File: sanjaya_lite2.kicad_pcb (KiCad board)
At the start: 2 copper layers, 104 parts, among them J1 Conn_12V, J10 Adap_In, J11 DCDC_Bypass, J12 Conn_RS485, J13 Bat_Bypass+, J14 J_Bat, J15 Conn_420_1, J16 Conn_420_2, J17 Conn_420_3, J18 Conn_420_4, J19 Volt_check_5V, J2 J_SW_Esp, J20 Pwr_SW, J21 J_SW_Sim800, J3 Conn_5V, J4 J_LED, J5 Conn_Bat, J6 Conn_I2C, J7 Conn_SPI, J8 Conn_I2C, J9 J_UART_DBG, Q1 PMOS_SI2369DS, Q2 BSS138, Q3 BSS138, SW1 SW_Reset, SW2 SW_Boot, U1 ESP32-WROOM-32, U2 MCP1700-3302E_SOT23, U3 SN65HVD75DR, U5 MCP3428

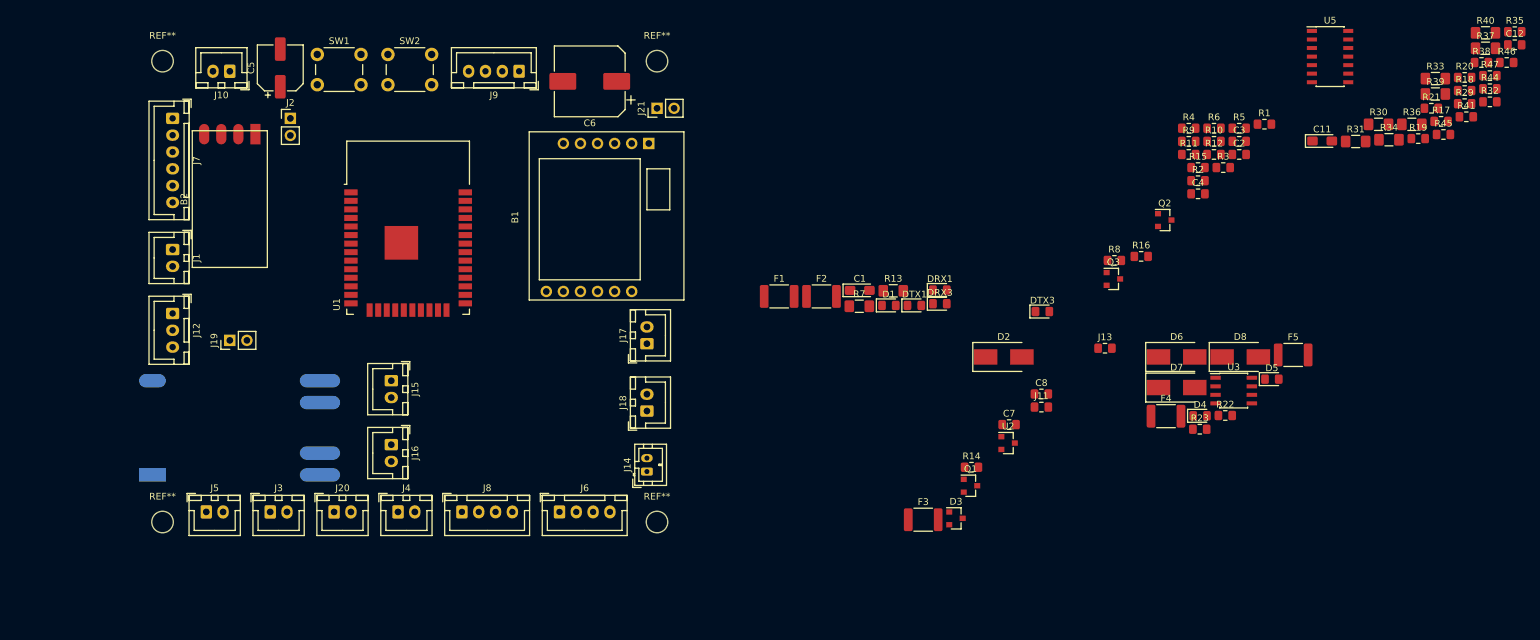
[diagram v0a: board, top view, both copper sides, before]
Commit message: Basic board layout with connectors and large components done
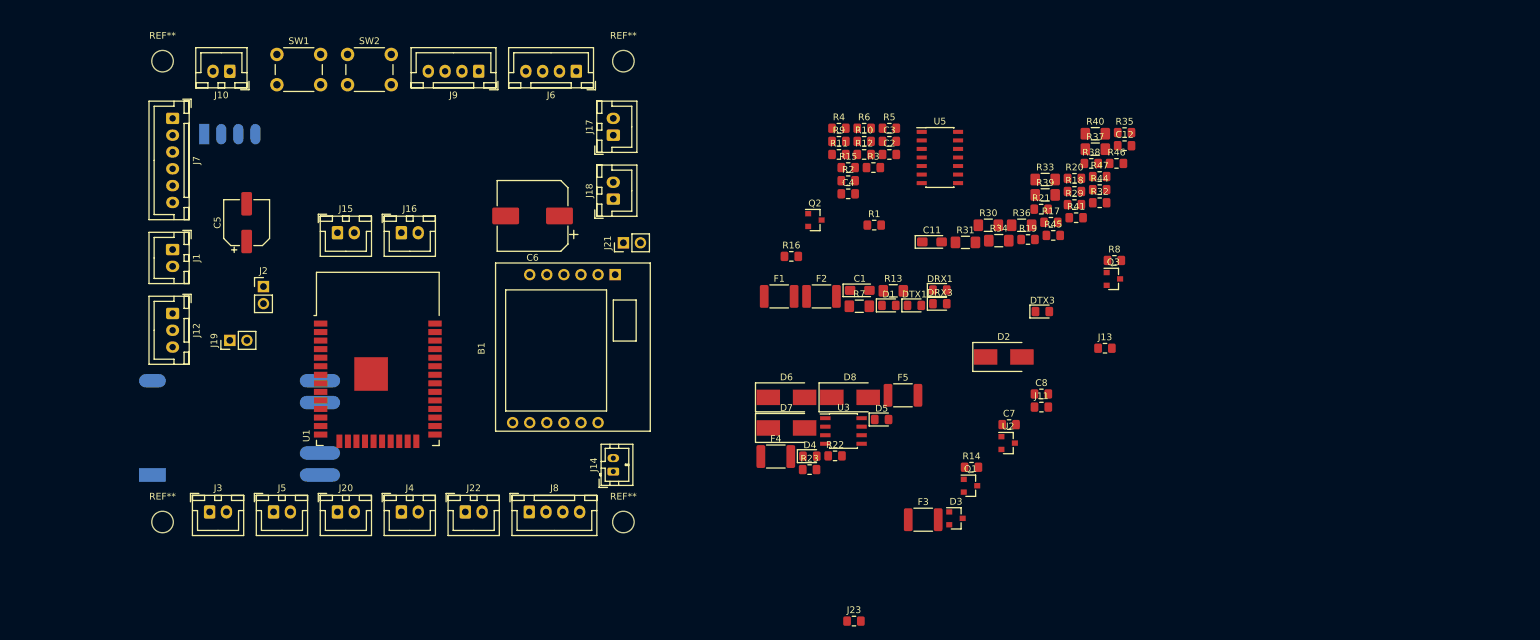
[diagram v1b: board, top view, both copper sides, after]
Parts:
- added J22: UART_Sim800, Connector_JST:JST_XH_B02B-XH-A_1x02_P2.50mm_Vertical, F.Cu at (135.0, 127.0)
- added J23: Bat_Prot_Bypass, Resistor_SMD:R_0805_2012Metric_Pad1.15x1.40mm_HandSolder, F.Cu at (192.8, 143.2)
- B2: moved to B.Cu
- J1: value Conn_12V -> 12V_Out
- J13: value Bat_Bypass+ -> Bat_Bypass
- J3: value Conn_5V -> 5V_Out
- J5: value Conn_Bat -> VBat_Out
- moved J6 65.5 mm to (151.5, 61.5), turned to 180 degrees
- moved C11 59.9 mm to (204.4, 86.9)
- moved R17 59.9 mm to (222.0, 83.9)
- moved R18 59.9 mm to (225.5, 79.4)
- moved R20 59.9 mm to (225.5, 77.4)
- moved R29 59.9 mm to (225.5, 81.3)
- moved R32 59.9 mm to (229.3, 81.0)
- moved R34 59.9 mm to (214.3, 86.7)
- moved R38 59.9 mm to (228.0, 75.2)
- moved R41 59.9 mm to (225.8, 83.3)
- moved R44 59.9 mm to (229.3, 79.1)
- moved R46 59.9 mm to (231.8, 75.2)
- moved R47 59.9 mm to (229.3, 77.1)
- moved U5 59.9 mm to (205.5, 74.3)
- moved C12 59.9 mm to (233.0, 72.6)
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
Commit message: Made some changes to the layout. It is still incomplete
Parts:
- added G***: LOGO, Custom Silkscreens:bodhileafLogoAndText, F.Cu at (121.0, 119.4)
- added R24: 120, Resistor_SMD:R_0805_2012Metric_Pad1.15x1.40mm_HandSolder, F.Cu at (74.0, 106.5)
- added REF**: TestPoint_THTPad_D2.0mm_Drill1.0mm, TestPoint:TestPoint_THTPad_D2.0mm_Drill1.0mm, F.Cu at (110.5, 106.0)
- C1, C2, C3, C4, R1, R13, R2, R3, R4, R5, R6: moved to B.Cu
- U1: footprint RF_Module:ESP32-WROOM-32 -> Custom Boards:ESP32-WROOM-32_Handsolder
- moved D6 110.6 mm to (72.5, 101.0)
- moved D1 98.5 mm to (99.5, 100.0), turned to 90 degrees
- moved C1 97.8 mm to (96.0, 100.5), turned to 270 degrees
- moved R1 94.6 mm to (102.5, 100.0), turned to 270 degrees
- moved C2 94.2 mm to (107.5, 100.0), turned to 270 degrees
- moved R3 92.9 mm to (106.0, 100.0), turned to 270 degrees
- moved R5 91.9 mm to (116.5, 112.5), turned to 270 degrees
- moved R6 91.3 mm to (113.5, 112.5), turned to 90 degrees
- moved C3 90.5 mm to (112.0, 100.0), turned to 270 degrees
- moved C4 87.8 mm to (110.5, 112.5), turned to 270 degrees
- moved R4 86.9 mm to (109.0, 100.0), turned to 90 degrees
- moved DTX3 86.9 mm to (134.0, 93.0), turned to 90 degrees
- moved Q3 86.5 mm to (145.4, 101.7)
- moved R2 75.0 mm to (129.5, 119.4), turned to 270 degrees
- moved F5 71.5 mm to (129.5, 121.0)
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
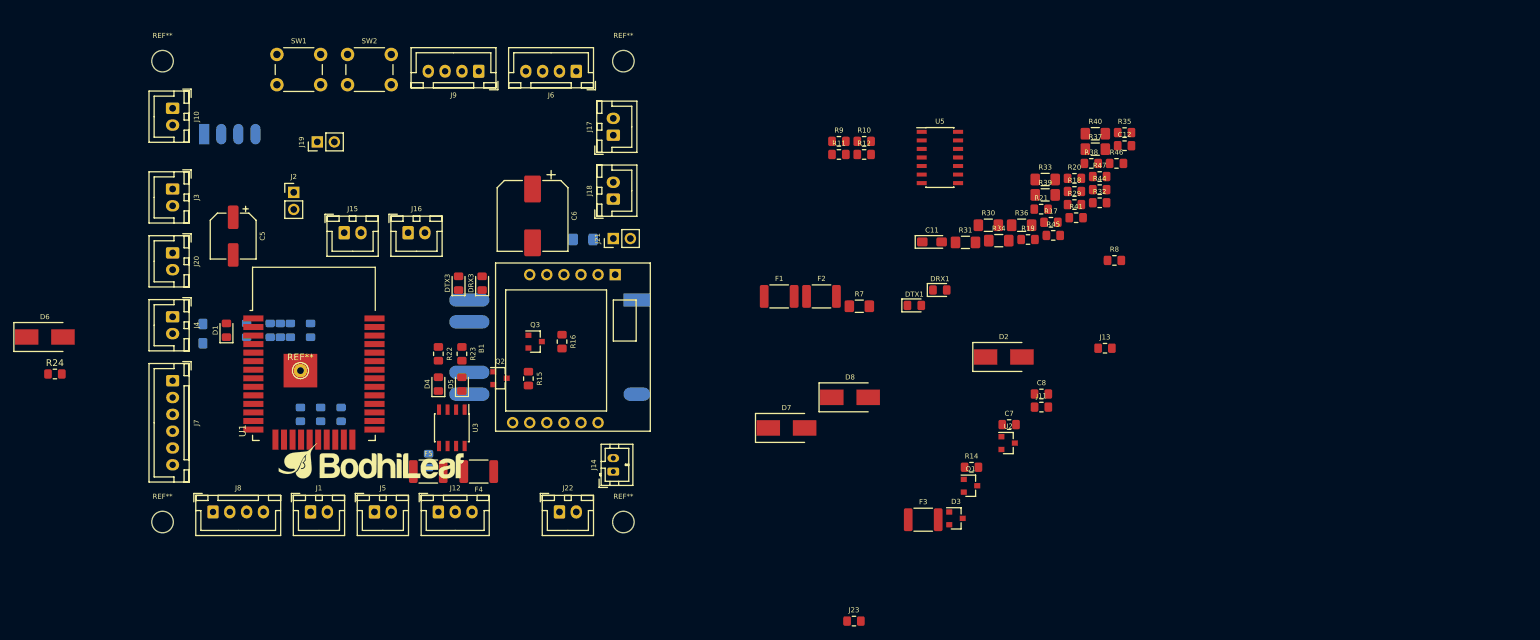
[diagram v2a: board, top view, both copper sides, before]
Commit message: Most of the layout done. Some power supply related components are the only ones remaining
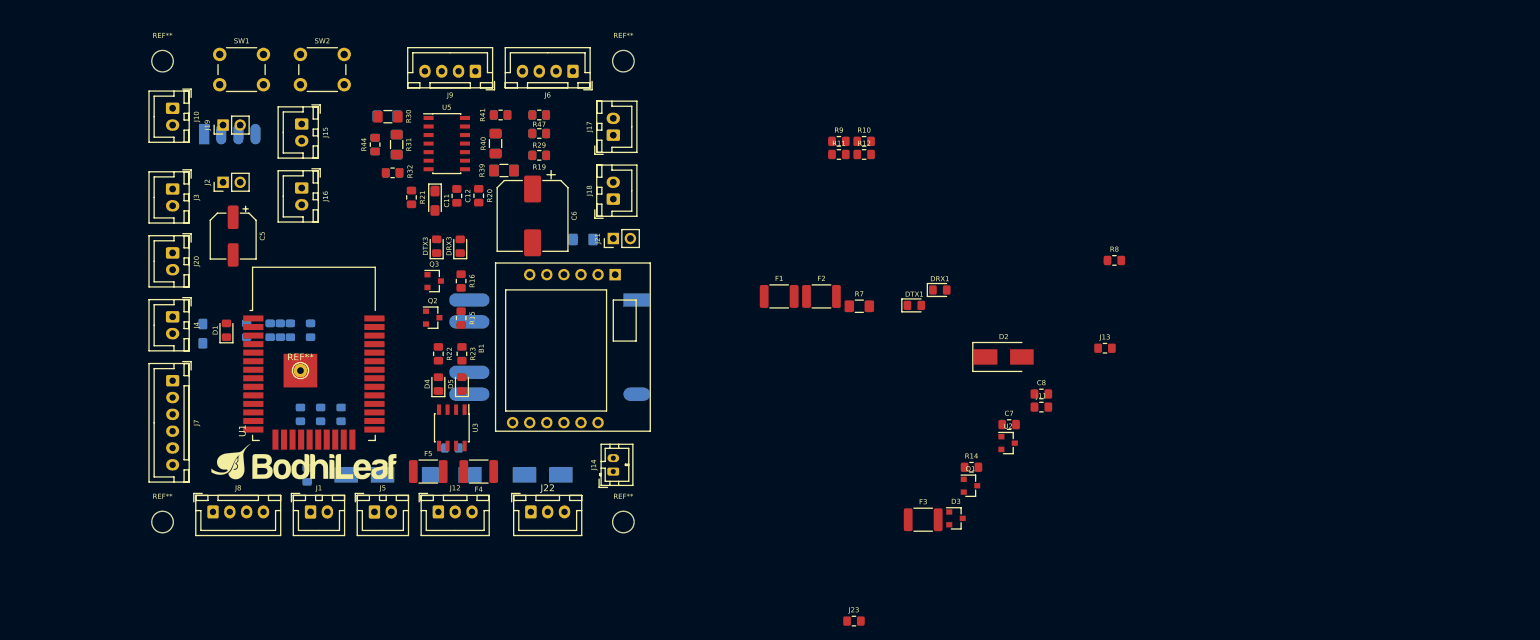
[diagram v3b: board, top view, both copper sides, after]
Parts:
- D6, D7, D8, R17, R18, R24, R33, R34, R35, R36, R37, R38, R45, R46: moved to B.Cu
- J22: footprint Connector_JST:JST_XH_B02B-XH-A_1x02_P2.50mm_Vertical -> Connector_JST:JST_XH_B03B-XH-A_1x03_P2.50mm_Vertical
- moved R35 109.0 mm to (124.2, 76.6)
- moved R44 107.9 mm to (121.6, 72.4), turned to 90 degrees
- moved R32 105.2 mm to (124.2, 76.6)
- moved R45 101.7 mm to (121.6, 72.4), turned to 270 degrees
- moved C12 99.5 mm to (133.8, 80.0), turned to 270 degrees
- moved R33 98.2 mm to (123.4, 68.2)
- moved R21 93.6 mm to (127.0, 80.2), turned to 270 degrees
- moved R30 90.7 mm to (123.5, 68.2)
- moved R34 90.6 mm to (124.8, 72.4), turned to 270 degrees
- moved R40 89.2 mm to (139.5, 72.2), turned to 90 degrees
- moved R37 89.2 mm to (139.5, 72.2), turned to 90 degrees
- moved R20 88.6 mm to (137.0, 80.0), turned to 270 degrees
- moved R38 88.1 mm to (140.2, 68.0)
- moved R41 86.9 mm to (140.2, 68.0)
- moved R46 86.1 mm to (146.0, 68.0)
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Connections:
- J22 pad 1: Net-(J22-Pad1) -> /GND_Supply
- Q3 pad 3: Net-(J22-Pad1) -> Net-(J22-Pad3)
- U1 pad 13: Net-(J22-Pad1) -> Net-(J22-Pad3)

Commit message: First layout draft
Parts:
- C7, C8, D3, F1, F2, J11, J13, J23, Q1, R10, R11, R12, R14, R7, R8, U2: moved to B.Cu
- moved R8 135.6 mm to (96.0, 95.5), turned to 270 degrees
- moved J13 135.4 mm to (96.5, 80.5), turned to 90 degrees
- moved J11 124.5 mm to (100.0, 80.5), turned to 270 degrees
- moved F3 118.8 mm to (100.0, 69.0), turned to 180 degrees
- moved D2 118.8 mm to (100.0, 74.5)
- moved Q1 115.1 mm to (108.0, 70.0), turned to 90 degrees
- moved D3 113.8 mm to (108.0, 73.5), turned to 180 degrees
- moved R14 111.3 mm to (108.0, 76.5), turned to 180 degrees
- moved R9 101.5 mm to (97.5, 112.5), turned to 180 degrees
- moved R7 96.5 mm to (98.0, 109.5)
- moved C8 95.7 mm to (125.0, 112.0), turned to 180 degrees
- moved R12 94.3 mm to (107.0, 109.5), turned to 90 degrees
- moved C7 91.3 mm to (125.0, 105.0), turned to 180 degrees
- moved U2 91.1 mm to (125.0, 108.5)
- moved DRX1 82.3 mm to (123.5, 87.5), turned to 90 degrees
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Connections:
- DRX3 pad 1: Net-(B1-Pad5) -> Net-(DRX3-Pad1)
- DRX3 pad 2: Net-(DRX3-Pad2) -> Net-(B1-Pad12)
- DTX3 pad 1: Net-(B1-Pad4) -> Net-(DTX3-Pad1)
- DTX3 pad 2: Net-(DTX3-Pad2) -> Net-(B1-Pad12)
- R15 pad 1: Net-(B1-Pad12) -> Net-(DTX3-Pad1)
- R15 pad 2: Net-(DTX3-Pad2) -> Net-(B1-Pad4)
- R16 pad 1: Net-(B1-Pad12) -> Net-(DRX3-Pad1)
- R16 pad 2: Net-(DRX3-Pad2) -> Net-(B1-Pad5)

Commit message: Created a 1A net class
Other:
- net class 1A_Carrier added: clearance 0.4, trace_width 0.5, via_dia 1, via_drill 0.5
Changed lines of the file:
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@@
     (37 F.SilkS user)
     (38 B.Mask user)
-    (39 F.Mask user)
+    (39 F.Mask user hide)
     (40 Dwgs.User user)
     (41 Cmts.User user)
@@
     (45 Margin user)
     (46 B.CrtYd user)
-    (47 F.CrtYd user)
+    (47 F.CrtYd user hide)
     (48 B.Fab user)
     (49 F.Fab user)
@@
     (solder_mask_min_width 0.25)
     (aux_axis_origin 0 0)
-    (visible_elements FFFFF77F)
+    (visible_elements FFFFFF7F)
     (pcbplotparams
       (layerselection 0x010fc_ffffffff)
@@
     (uvia_dia 0.3)
     (uvia_drill 0.1)
-    (add_net /12V_Out)
-    (add_net /5V_Out)
     (add_net /BOOT_IO0)
     (add_net /BOOT_IO2)
@@
     (add_net /SCLK)
     (add_net /SDA)
-    (add_net /Sim800_I_Sense+)
-    (add_net /Sim800_I_Sense-)
     (add_net /Sim800_RST)
     (add_net /rs485/A)
@@
     (add_net "Net-(B1-Pad5)")
     (add_net "Net-(B2-Pad3)")
-    (add_net "Net-(B2-Pad4)")
-    (add_net "Net-(B3-Pad4)")
-    (add_net "Net-(B3-Pad5)")
-    (add_net "Net-(B3-Pad6)")
     (add_net "Net-(C3-Pad1)")
     (add_net "Net-(C4-Pad1)")
     (add_net "Net-(D1-Pad2)")
-    (add_net "Net-(D2-Pad1)")
     (add_net "Net-(D3-Pad2)")
     (add_net "Net-(D4-Pad2)")
@@
     (add_net "Net-(DTX1-Pad2)")
     (add_net "Net-(DTX3-Pad1)")
-    (add_net "Net-(F1-Pad2)")
-    (add_net "Net-(F2-Pad2)")
-    (add_net "Net-(F3-Pad2)")
     (add_net "Net-(F4-Pad2)")
     (add_net "Net-(F5-Pad2)")
@@
     (add_net "Net-(R33-Pad2)")
   )
+  (net_class 1A_Carrier ""
+    (clearance 0.4)
+    (trace_width 0.5)
+    (via_dia 1)
+    (via_drill 0.5)
+    (uvia_dia 0.3)
+    (uvia_drill 0.1)
+    (add_net /12V_Out)
+    (add_net /5V_Out)
+    (add_net /Sim800_I_Sense+)
+    (add_net /Sim800_I_Sense-)
+    (add_net "Net-(B2-Pad4)")
+    (add_net "Net-(B3-Pad4)")
+    (add_net "Net-(B3-Pad5)")
+    (add_net "Net-(B3-Pad6)")
+    (add_net "Net-(D2-Pad1)")
+    (add_net "Net-(F1-Pad2)")
+    (add_net "Net-(F2-Pad2)")
+    (add_net "Net-(F3-Pad2)")
+  )
   (module "Custom Boards:TP4056_Module" (layer B.Cu)

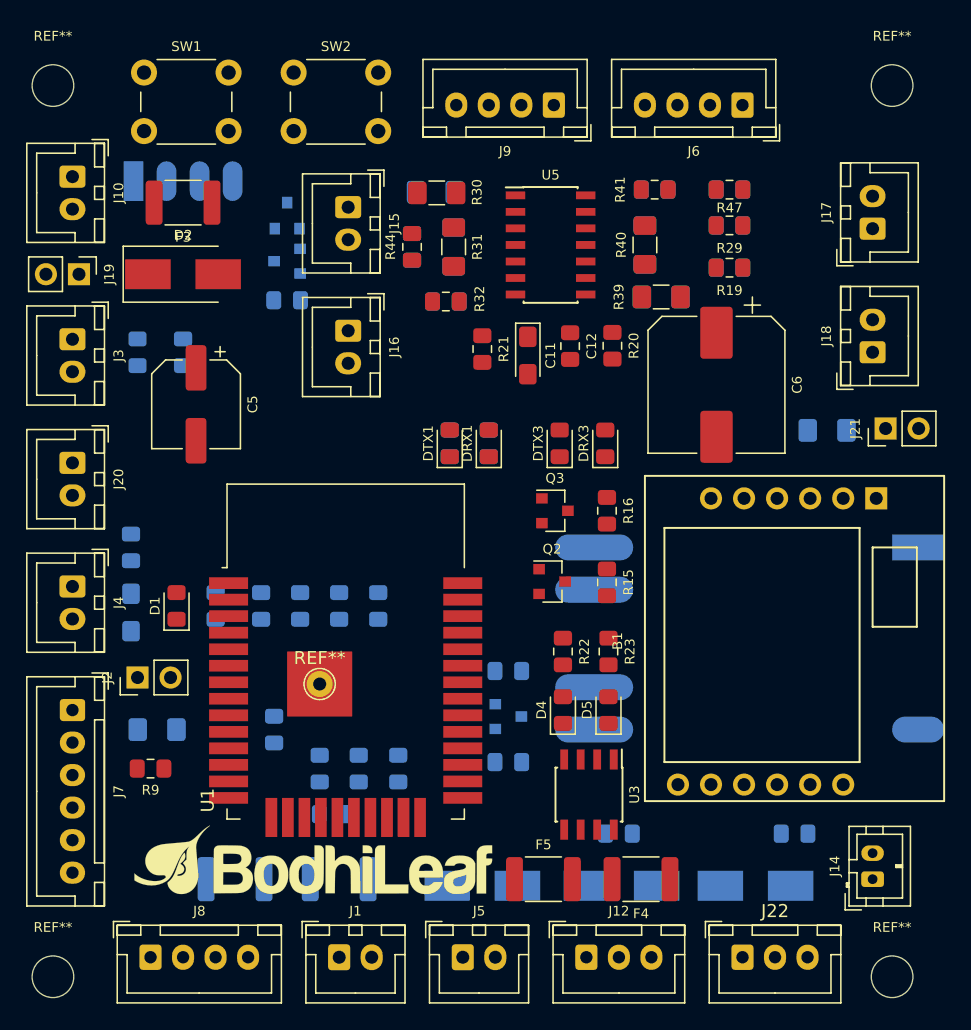
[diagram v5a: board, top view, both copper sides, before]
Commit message: Some routing done. Minor changes to schematics.
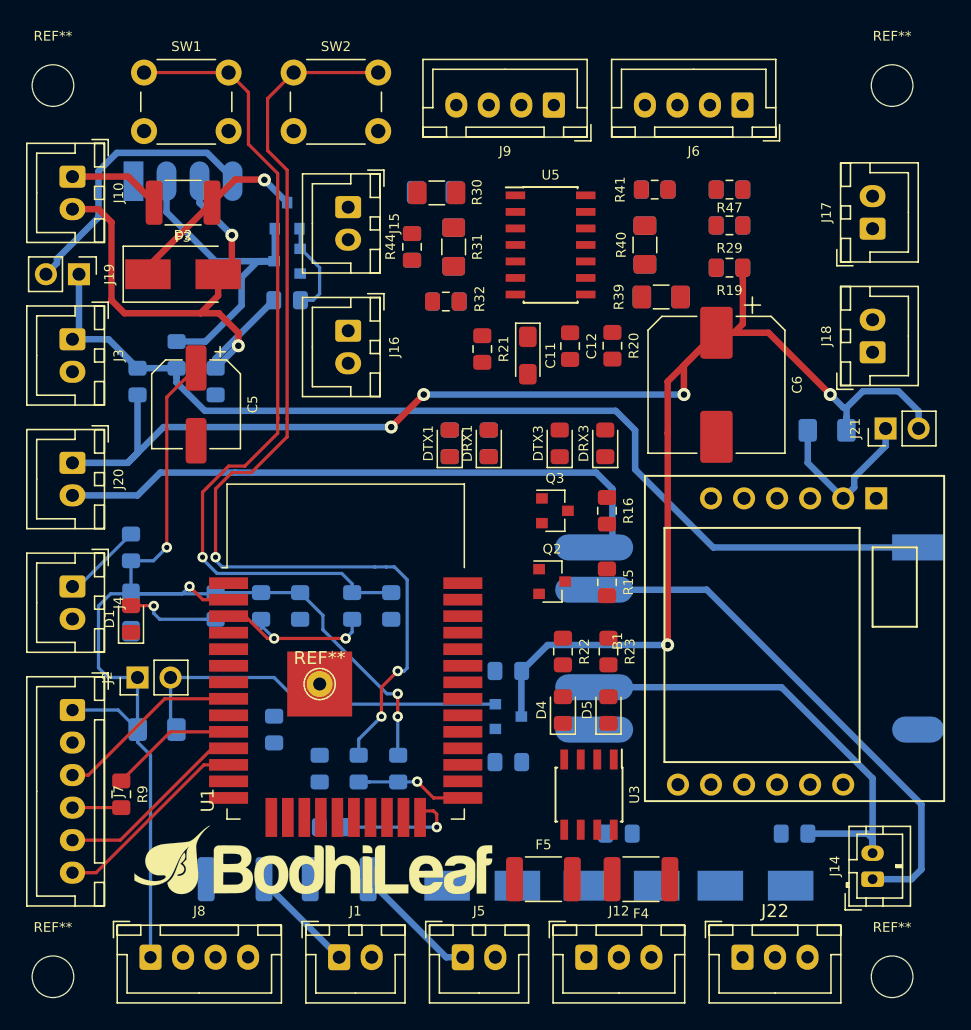
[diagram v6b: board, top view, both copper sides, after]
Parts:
- added J24: Bat_Bypass-, Resistor_SMD:R_0805_2012Metric_Pad1.15x1.40mm_HandSolder, B.Cu at (102.5, 82.8)
- D2, D6, D7, D8: value TVS_SMBJ20CA -> TVS_SMBJ30CA
- J13: value Bat_Bypass -> Bat_Bypass+
- moved D1 3.64 mm to (96.0, 101.0)
- moved R9 2.99 mm to (95.2, 114.5), turned to 270 degrees
- moved J13 2.25 mm to (96.5, 82.8)
- moved C3 1.00 mm to (116.0, 100.0)
- moved R2 1.00 mm to (111.5, 117.0)
- moved R4 1.00 mm to (113.0, 100.0)
- moved J11 0.54 mm to (99.5, 80.7), turned to 90 degrees
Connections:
- J7 pad 3: Net-(J7-Pad3) -> /CS
- J7 pad 4: /MISO_RLY1 -> Net-(J7-Pad4)
- J7 pad 5: /MOSI_RLY2 -> /MISO_RLY1
- J7 pad 6: /CS -> /MOSI_RLY2
- R9 pad 2: Net-(J7-Pad3) -> Net-(J7-Pad4)
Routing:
- net /Sim800_I_Sense+: track 0.00 -> 130.4 mm, vias 0 -> 5
- net /Esp_I_Sense+: track 0.00 -> 96.7 mm, vias 0 -> 4
- net Net-(C4-Pad1): track 0.00 -> 79.3 mm, vias 0 -> 3
- net /5V_Out: track 0.00 -> 78.7 mm
- net Net-(C3-Pad1): track 0.00 -> 64.8 mm, vias 0 -> 1
- net Net-(B3-Pad6): track 0.00 -> 47.2 mm
- net Net-(B2-Pad3): track 0.00 -> 42.2 mm, vias 0 -> 2
- net Net-(B3-Pad5): track 0.00 -> 39.6 mm
- net Net-(B3-Pad4): track 0.00 -> 34.9 mm
- net /Esp_I_Sense-: track 0.00 -> 30.0 mm
- net /12V_Out: track 0.00 -> 25.3 mm
- net Net-(B2-Pad4): track 0.00 -> 22.3 mm
- net /MOSI_RLY2: track 0.00 -> 15.9 mm
- net /MISO_RLY1: track 0.00 -> 15.4 mm
- net /CS: track 0.00 -> 14.9 mm
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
